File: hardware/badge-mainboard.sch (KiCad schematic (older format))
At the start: 14 parts

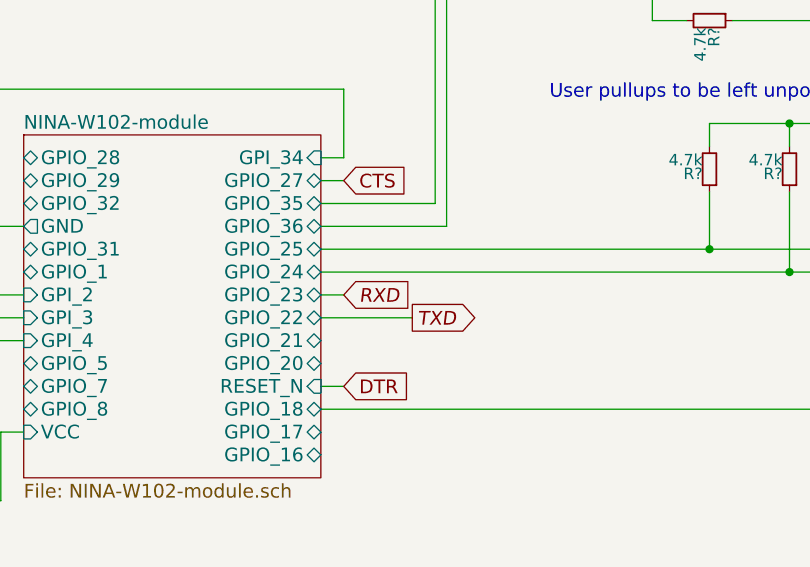
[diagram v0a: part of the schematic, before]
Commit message: cleaned programmer on carrier board
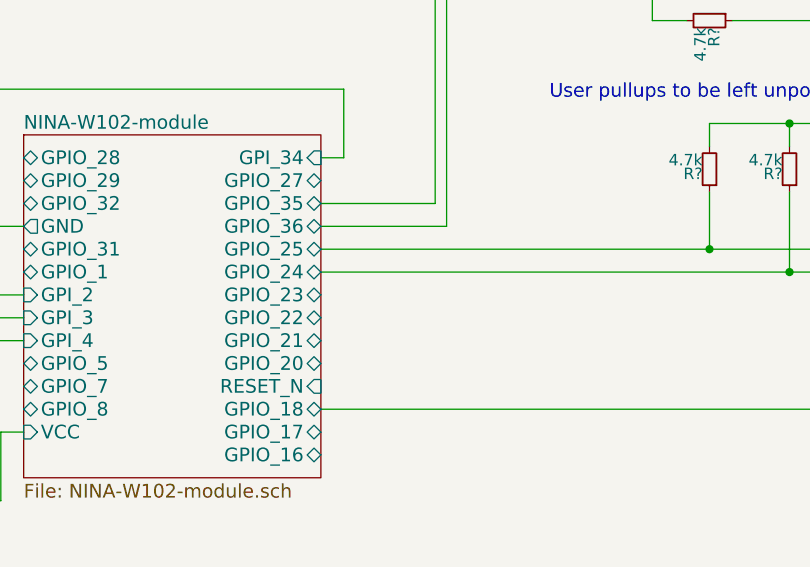
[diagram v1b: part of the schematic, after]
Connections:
- net labels removed: CTS, DTR, RXD, TXD
- wire segments 80 -> 76
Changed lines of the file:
@@
 Sheet 1 5
 Title "IoT conference badge - mainboard"
-Date "2018-04-09"
-Rev "0.2.0"
+Date "2018-05-17"
+Rev "0.3.0"
 Comp "MakeZürich (makezurich.ch) & GDG Zürich (gdgzh.ch)"
 Comment1 ""
@@
 Text Notes 10100 1850 2    60   ~ 0
 I2C Breakouts for users
-Text GLabel 6500 2550 2    60   Output Italic 0
-TXD
-Text GLabel 6200 2450 2    60   Input Italic 0
-RXD
-Text GLabel 6200 1950 2    60   Input ~ 0
-CTS
-Text GLabel 6200 2850 2    60   Input ~ 0
-DTR
 $Sheet
 S 2550 2250 1150 650
@@
 	10150 2550 8950 2550
 Wire Wire Line
-	6200 1950 6100 1950
-Wire Wire Line
-	6200 2850 6100 2850
-Wire Wire Line
-	6200 2450 6100 2450
-Wire Wire Line
-	6500 2550 6100 2550
-Wire Wire Line
 	4800 2450 3700 2450

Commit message: Added SPI connection for EPD
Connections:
- wire segments 76 -> 94
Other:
- note added: "Needs to be tested first, not sure about the pins"
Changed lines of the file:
@@
 	9750 1250 9750 850
 Connection ~ 9750 850
+Wire Wire Line
+	4800 2350 4000 2350
+Wire Wire Line
+	4000 2350 4000 4800
+Wire Wire Line
+	4000 4800 5050 4800
+Wire Wire Line
+	5100 4900 3950 4900
+Wire Wire Line
+	3950 4900 3950 1950
+Wire Wire Line
+	3950 1950 4800 1950
+Wire Wire Line
+	4800 1850 2350 1850
+Wire Wire Line
+	2350 1850 2350 5000
+Wire Wire Line
+	2350 5000 5050 5000
+$Comp
+L GND #PWR?
+U 1 1 5B015D33
+P 2800 5150
+F 0 "#PWR?" H 2800 4900 50  0001 C CNN
+F 1 "GND" H 2800 5000 50  0000 C CNN
+F 2 "" H 2800 5150 50  0001 C CNN
+F 3 "" H 2800 5150 50  0001 C CNN
+	1    2800 5150
+	1    0    0    -1
+$EndComp
+Wire Wire Line
+	2800 5150 2800 5100
+Wire Wire Line
+	2800 5100 5050 5100
+$Comp
+L +3V3 #PWR?
+U 1 1 5B017B96
+P 2500 5450
+F 0 "#PWR?" H 2500 5300 50  0001 C CNN
+F 1 "+3V3" H 2500 5590 50  0000 C CNN
+F 2 "" H 2500 5450 50  0001 C CNN
+F 3 "" H 2500 5450 50  0001 C CNN
+	1    2500 5450
+	1    0    0    -1
+$EndComp
+Wire Wire Line
+	2500 5450 2500 5550
+Wire Wire Line
+	2500 5550 3200 5550
+Wire Wire Line
+	3200 5550 3200 5200
+Wire Wire Line
+	3200 5200 5050 5200
+Wire Wire Line
+	4800 2950 3850 2950
+Wire Wire Line
+	3850 2950 3850 5300
+Wire Wire Line
+	3850 5300 5050 5300
+Text Notes 7050 4450 2    60   ~ 0
+Needs to be tested first, not sure about the pins
 $EndSCHEMATC

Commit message: moved connections
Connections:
- wire segments 94 -> 96
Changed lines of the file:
@@
 F3 "CLK" I L 5050 4900 60
 F4 "CS" I L 5050 5000 60
-F5 "DC" I L 5050 5100 60
-F6 "RST" I L 5050 5200 60
-F7 "BUSY" O L 5050 5300 60
+F5 "DC" I R 6750 5350 60
+F6 "RST" I R 6750 4800 60
+F7 "BUSY" O L 5050 4700 60
+F8 "GND" O R 6750 5200 60
+F9 "VCC" I R 6750 4950 60
 $EndSheet
 $Sheet
@@
 	4000 4800 5050 4800
 Wire Wire Line
-	5100 4900 3950 4900
-Wire Wire Line
 	3950 4900 3950 1950
 Wire Wire Line
@@
 Wire Wire Line
 	2350 5000 5050 5000
-$Comp
-L GND #PWR?
-U 1 1 5B015D33
-P 2800 5150
-F 0 "#PWR?" H 2800 4900 50  0001 C CNN
-F 1 "GND" H 2800 5000 50  0000 C CNN
-F 2 "" H 2800 5150 50  0001 C CNN
-F 3 "" H 2800 5150 50  0001 C CNN
-	1    2800 5150
-	1    0    0    -1
-$EndComp
-Wire Wire Line
-	2800 5150 2800 5100
-Wire Wire Line
-	2800 5100 5050 5100
-$Comp
-L +3V3 #PWR?
-U 1 1 5B017B96
-P 2500 5450
-F 0 "#PWR?" H 2500 5300 50  0001 C CNN
-F 1 "+3V3" H 2500 5590 50  0000 C CNN
-F 2 "" H 2500 5450 50  0001 C CNN
-F 3 "" H 2500 5450 50  0001 C CNN
-	1    2500 5450
-	1    0    0    -1
-$EndComp
-Wire Wire Line
-	2500 5450 2500 5550
-Wire Wire Line
-	2500 5550 3200 5550
-Wire Wire Line
-	3200 5550 3200 5200
-Wire Wire Line
-	3200 5200 5050 5200
-Wire Wire Line
-	4800 2950 3850 2950
-Wire Wire Line
-	3850 2950 3850 5300
-Wire Wire Line
-	3850 5300 5050 5300
 Text Notes 7050 4450 2    60   ~ 0
 Needs to be tested first, not sure about the pins
+$Comp
+L +3V3 #PWR?
+U 1 1 5B01D407
+P 7150 4800
+F 0 "#PWR?" H 7150 4650 50  0001 C CNN
+F 1 "+3V3" H 7150 4940 50  0000 C CNN
+F 2 "" H 7150 4800 50  0001 C CNN
+F 3 "" H 7150 4800 50  0001 C CNN
+	1    7150 4800
+	1    0    0    -1
+$EndComp
+$Comp
+L GND #PWR?
+U 1 1 5B01D538
+P 7200 5350
+F 0 "#PWR?" H 7200 5100 50  0001 C CNN
+F 1 "GND" H 7200 5200 50  0000 C CNN
+F 2 "" H 7200 5350 50  0001 C CNN
+F 3 "" H 7200 5350 50  0001 C CNN
+	1    7200 5350
+	1    0    0    -1
+$EndComp
+Wire Wire Line
+	6750 4950 7150 4950
+Wire Wire Line
+	7150 4950 7150 4800
+Wire Wire Line
+	6750 5200 7200 5200
+Wire Wire Line
+	7200 5200 7200 5350
+Wire Wire Line
+	6750 4800 6950 4800
+Wire Wire Line
+	6950 4800 6950 4950
+Connection ~ 6950 4950
+Wire Wire Line
+	6750 5350 6950 5350
+Wire Wire Line
+	6950 5350 6950 5200
+Connection ~ 6950 5200
+Wire Wire Line
+	5050 4700 4250 4700
+Wire Wire Line
+	4250 4700 4250 2950
+Wire Wire Line
+	4250 2950 4800 2950
+Wire Wire Line
+	5050 4900 3950 4900
 $EndSCHEMATC

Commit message: added initial power circuit
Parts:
- added BT?: Battery 3x1.5V AAA, symbol Battery
- added C? (x2): 10uF (Tantalum), symbol C_Small
- added D?: D_Small, symbol D_Small
- added J? (x2): Vin, symbol Conn_01x02
- added U?: LM1117-3.3, symbol LM1117-3.3
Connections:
- net labels removed: +1V8
- wire segments 96 -> 109
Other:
- note added: "180mA max."
- note added: "500mA max. power consumption"
- note added: "Assume 20mA to 30mA max."
- note added: "Power circuit"

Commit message: Finished first complete revision for badge carrier board schematic
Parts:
- removed C?: 100nF, symbol C_Small
- removed LED?: WS2812b, WS2812B_1, symbol WS2812b
- added C1, C2, C3, C5: 1uF, symbol C_Small
- added J3: Rpi_02x20_WaveShareEPD, symbol Rpi_02x20_WaveShareEPD
- added R1, R2, R3, R4: 10k, symbol R_Small
- added SW1: User Button 2, symbol SW_Push
- added SW2: User Button 1, symbol SW_Push
- added SW3: User Button 3, symbol SW_Push
- added SW4: User Button 4, symbol SW_Push
- gave numbers to parts that had none: 19
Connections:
- net GND is gone; now on net +3V3: BT1.2 (-), C4.2, C6.2, C7.2, C8.2, C9.2, J1.1 (Pin_1), J2.1 (Pin_1), J4.GND, J5.GND, LED1.3 (VSS), LED2.3 (VSS), U1.1 (GND), U2.2 (GND)
- net +3V3: now also C1.2, C2.2, C3.2, C5.2, J3.GND (Pin_20), J3.VCC (Pin_1), R1.1, R2.1, R3.1, R4.1, SW1.1, SW2.1, SW3.1, SW4.1
- net NINA-W102-module/GPIO_20: now also J3.DC (Pin_31)
- net NINA-W102-module/GPIO_24: now also J3.BUSY (Pin_29); no longer J4.SDA, J5.SDA, R8.1
- net NINA-W102-module/GPIO_25: now also J4.SDA, J5.SDA, R8.1; no longer J4.SCL, J5.SCL, R7.1
- net NINA-W102-module/GPIO_27: now also R5.1, U2.3 (SCL)
- net NINA-W102-module/GPIO_36: now also J4.SCL, J5.SCL, R7.1; no longer R5.1, U2.3 (SCL)
- net NINA-W102-module/GPI_2: now also C1.1, R1.2, SW1.2
- net NINA-W102-module/GPI_3: now also C3.1, R3.2, SW3.2
- net NINA-W102-module/GPI_34: now also C2.1, R2.2, SW2.2
- net NINA-W102-module/GPI_4: now also C5.1, R4.2, SW4.2
- net at LED1.2 (DOUT): now also LED2.4 (DIN)
- net +BATT: now reaches BT1.1 (+), D1.2 (A), J1.2 (Pin_2), J2.2 (Pin_2)
- new net NINA-W102-module/GPIO_1: J3.DIN (Pin_10)
- new net NINA-W102-module/GPIO_28: J3.CS (Pin_32)
- new net NINA-W102-module/GPIO_29: J3.CLK (Pin_12)
- new net NINA-W102-module/GPIO_8: J3.RST (Pin_6)
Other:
- note added: "120mA max. (60mA / LED)"
- note added: "DIN => GPIO1 => ESP32: 23 => Arduino: MOSI\nCLK => GPIO29 => ESP32: 18 => Arduino: SCK\nCS => GPIO28 => ESP32: 5 => Arduino: SS\nDC => GPIO20 => ESP32: 22 => Arduino: D6\nRST => GPIO8 => ESP32: 21 => Arduino: D18\nBUSY => GPIO24 => ESP32: 4 => Arduino: A10"
- note added: "EPD connector"
- note added: "User interactions"
- note added: "https://www.waveshare.com/wiki/2.13inch_e-Paper_HAT"
- note removed: "180mA max."
- moved on the sheet: BT1, C4, C6, C9, D1, J1, J2, J4, J5, LED2, R7, R8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

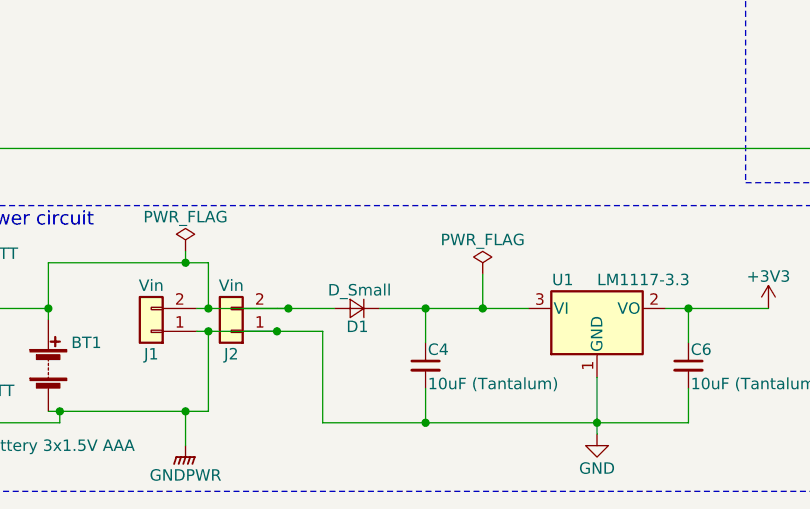
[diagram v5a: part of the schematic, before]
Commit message: Removed diode as not needed there
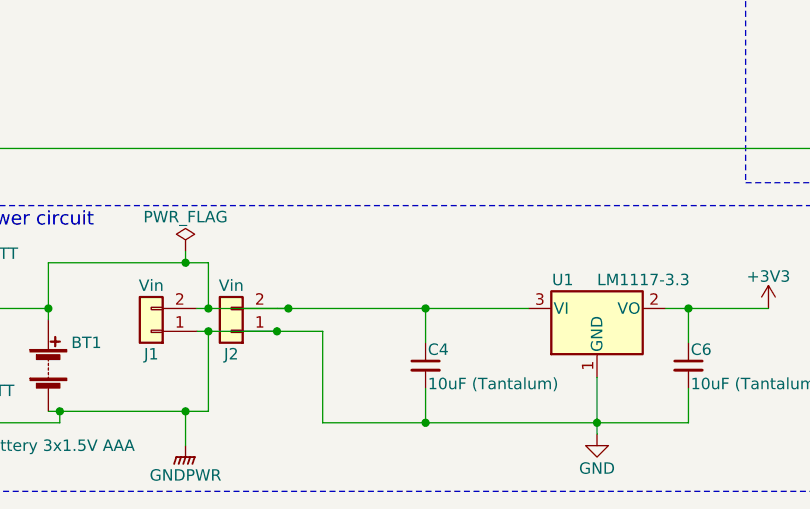
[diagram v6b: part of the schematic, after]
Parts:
- removed D1: D_Small, symbol D_Small
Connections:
- net +BATT: now also C4.1, U1.3 (VI)
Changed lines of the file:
@@
 Sheet 1 2
 Title "IoT conference badge - mainboard"
-Date "2018-05-19"
-Rev "0.3.2"
+Date "2018-05-20"
+Rev "0.3.3"
 Comp "MakeZürich (makezurich.ch) & GDG Zürich (gdgzh.ch)"
 Comment1 ""
@@
 $EndComp
 $Comp
-L D_Small D1
-U 1 1 5B02BB97
-P 2400 6900
-F 0 "D1" H 2350 6980 50  0000 L CNN
-F 1 "D_Small" H 2250 6820 50  0000 L CNN
-F 2 "" V 2400 6900 50  0001 C CNN
-F 3 "" V 2400 6900 50  0001 C CNN
-	1    2400 6900
-	-1   0    0    1
-$EndComp
-$Comp
 L Battery BT1
 U 1 1 5B02C983
@@
 	3850 7400 3850 7250
 Wire Wire Line
-	2500 6900 3150 6900
+	2050 6900 3150 6900
 Wire Wire Line
 	2700 6900 2700 7050
@@
 Connection ~ 1750 7000
 Wire Wire Line
-	2050 6900 2300 6900
-Wire Wire Line
 	1700 6900 2100 6900
 Connection ~ 2100 6900
@@
 	1650 6650 1650 6700
 Connection ~ 1650 6700
-Connection ~ 2950 6900
-Wire Wire Line
-	2950 6750 2950 6900
-$Comp
-L PWR_FLAG #FLG027
-U 1 1 5B050DA9
-P 2950 6750
-F 0 "#FLG027" H 2950 6825 50  0001 C CNN
-F 1 "PWR_FLAG" H 2950 6900 50  0000 C CNN
-F 2 "" H 2950 6750 50  0001 C CNN
-F 3 "" H 2950 6750 50  0001 C CNN
-	1    2950 6750
-	1    0    0    -1
-$EndComp
 Wire Wire Line
 	4350 2150 4800 2150

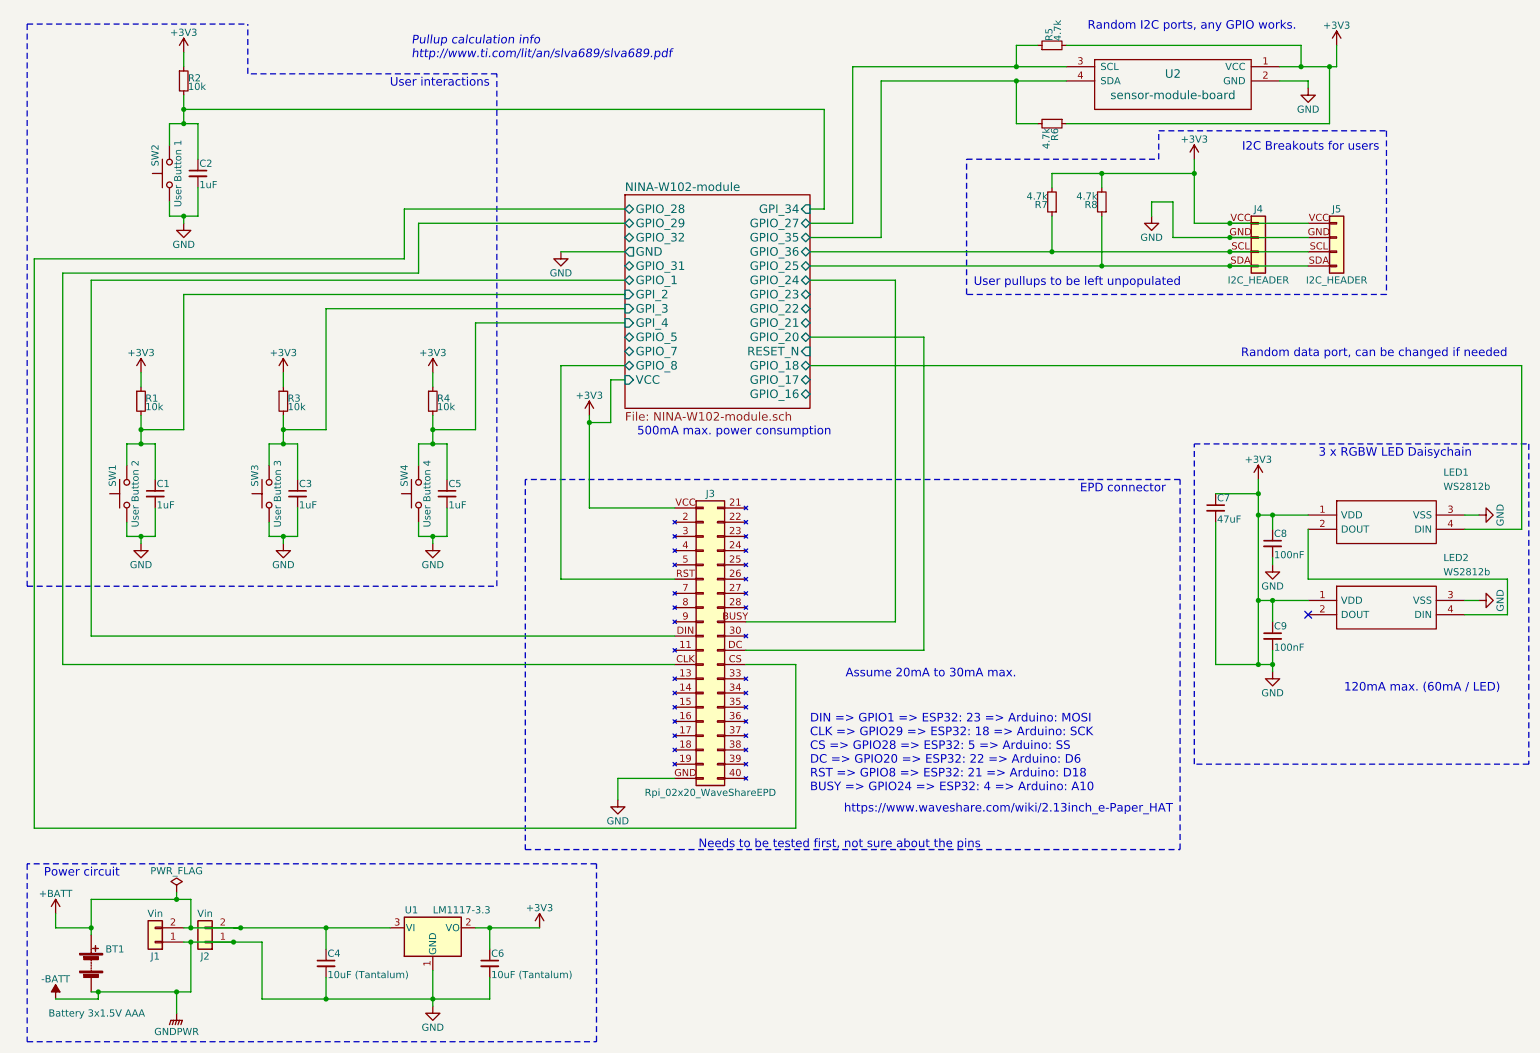
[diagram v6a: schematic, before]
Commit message: Added battery measurement trough ADC PIN and a voltage divider that is good up to 19V
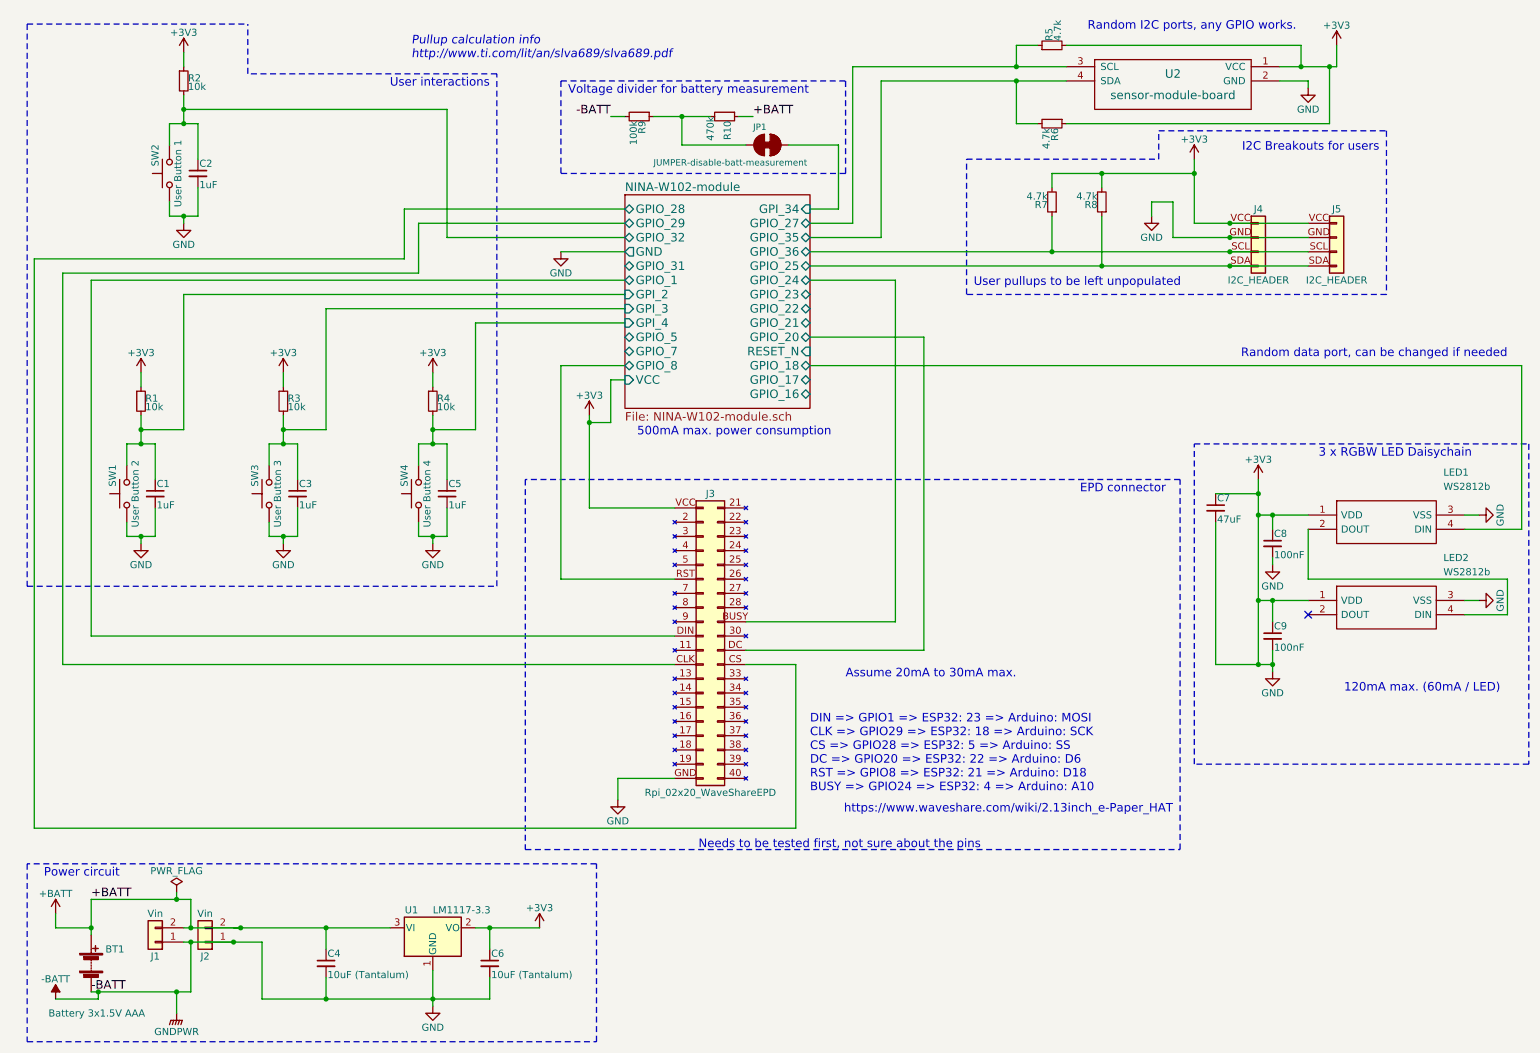
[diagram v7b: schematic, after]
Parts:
- added JP1: JUMPER-disable-batt-measurement, SMT-JUMPER_2_NC, symbol JUMPER-SMT_2_NC
- added R10: 470k, symbol R_Small
- added R9: 100k, symbol R_Small
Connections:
- net +3V3: now also R9.2
- net +BATT: now also R10.1
- net NINA-W102-module/GPIO_32: now also C2.1, R2.2, SW2.2
- net NINA-W102-module/GPI_34: now also JP1.2; no longer C2.1, R2.2, SW2.2
- new net: JP1.1, R10.2, R9.1
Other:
- note added: "Voltage divider for battery measurement"
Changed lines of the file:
@@
 	2700 2550 4800 2550
-Wire Wire Line
-	6200 1150 6200 1850
-Wire Wire Line
-	6200 1850 6100 1850
 Wire Wire Line
 	7800 1900 7800 2150
@@
 	1800 1250 1800 1500
 Connection ~ 1700 1250
-Wire Wire Line
-	1700 1150 6200 1150
 Connection ~ 1700 1150
 Wire Wire Line
@@
 Text Notes 3850 1000 2    60   ~ 0
 User interactions
+Wire Wire Line
+	1700 1150 3550 1150
+Wire Wire Line
+	3550 1150 3550 2050
+Wire Wire Line
+	3550 2050 4800 2050
+$Comp
+L R_Small R9
+U 1 1 5B00DCEE
+P 4900 1200
+F 0 "R9" H 4930 1220 50  0000 L CNN
+F 1 "100k" H 4930 1160 50  0000 L CNN
+F 2 "" H 4900 1200 50  0001 C CNN
+F 3 "" H 4900 1200 50  0001 C CNN
+	1    4900 1200
+	0    1    1    0
+$EndComp
+$Comp
+L R_Small R10
+U 1 1 5B00DF64
+P 5500 1200
+F 0 "R10" H 5530 1220 50  0000 L CNN
+F 1 "470k" H 5500 1100 50  0000 L CNN
+F 2 "" H 5500 1200 50  0001 C CNN
+F 3 "" H 5500 1200 50  0001 C CNN
+	1    5500 1200
+	0    1    1    0
+$EndComp
+Wire Wire Line
+	5000 1200 5400 1200
+Wire Wire Line
+	6100 1850 6300 1850
+Connection ~ 5200 1200
+Text Label 1050 6700 0    60   ~ 0
++BATT
+Text Label 1050 7350 0    60   ~ 0
+-BATT
+Text Label 5700 1200 0    60   ~ 0
++BATT
+Text Label 4700 1200 2    60   ~ 0
+-BATT
+Wire Wire Line
+	5600 1200 5700 1200
+Wire Wire Line
+	4800 1200 4700 1200
+Wire Notes Line
+	4350 950  4350 1600
+Wire Notes Line
+	4350 950  6350 950
+Text Notes 4400 1050 0    60   ~ 0
+Voltage divider for battery measurement
+$Comp
+L JUMPER-SMT_2_NC JP1
+U 1 1 5B0140EF
+P 5800 1400
+F 0 "JP1" H 5700 1500 45  0000 L BNN
+F 1 "JUMPER-disable-batt-measurement" H 5000 1250 45  0000 L BNN
+F 2 "SMT-JUMPER_2_NC" H 5800 1600 20  0001 C CNN
+F 3 "" H 5800 1400 60  0001 C CNN
+	1    5800 1400
+	1    0    0    -1
+$EndComp
+Wire Wire Line
+	5200 1200 5200 1400
+Wire Wire Line
+	5200 1400 5650 1400
+Wire Wire Line
+	5950 1400 6300 1400
+Wire Wire Line
+	6300 1400 6300 1850
+Wire Notes Line
+	6350 950  6350 1600
+Wire Notes Line
+	6350 1600 4350 1600
 $EndSCHEMATC

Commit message: Added zener for GPIO protection
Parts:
- added D1: D_Zener_3v3, symbol D_Zener_Small
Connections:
- net +3V3: now also D1.2 (A)
- net at JP1.1, R10.2, R9.1: now also D1.1 (K)
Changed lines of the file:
@@
 Title "IoT conference badge - mainboard"
 Date "2018-05-20"
-Rev "0.3.3"
+Rev "0.3.4"
 Comp "MakeZürich (makezurich.ch) & GDG Zürich (gdgzh.ch)"
 Comment1 ""
@@
 $EndComp
 Wire Wire Line
-	5200 1200 5200 1400
+	5200 1200 5200 1450
 Wire Wire Line
 	5200 1400 5650 1400
@@
 Wire Notes Line
 	6350 1600 4350 1600
+$Comp
+L D_Zener_Small D1
+U 1 1 5B0199E5
+P 4700 1450
+F 0 "D1" H 4700 1350 50  0000 C CNN
+F 1 "D_Zener_3v3" H 4700 1550 50  0000 C CNN
+F 2 "" V 4700 1450 50  0001 C CNN
+F 3 "" V 4700 1450 50  0001 C CNN
+	1    4700 1450
+	-1   0    0    1
+$EndComp
+Connection ~ 5200 1400
+Wire Wire Line
+	5200 1450 4800 1450
+Wire Wire Line
+	4600 1450 4600 1250
+Wire Wire Line
+	4600 1250 4750 1250
+Wire Wire Line
+	4750 1250 4750 1200
+Connection ~ 4750 1200
 $EndSCHEMATC
